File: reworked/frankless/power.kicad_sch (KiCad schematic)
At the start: 34 parts, among them J4 SS-52100-004, J5 USB4215-03-A, U1 TS3USB221RSER, U11 CH334R, U2 USBLC6-2SC6, U3 AMS1117-3.3, Y2 12Mhz, Y3 ASE-12MHz

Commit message: Patch a few minor issues.
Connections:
- net +3V3: no longer C39.2, C40.2, U11.13 (VDD33_{LDO})
- new net: C39.2, C40.2, U11.13 (VDD33_{LDO})
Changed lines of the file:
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@@
 	)
 	(junction
-		(at 130.81 110.49)
-		(diameter 0)
-		(color 0 0 0 0)
-	)
-	(junction
 		(at 27.94 123.19)
 		(diameter 0)
@@
 	(wire
 		(pts
-			(xy 129.54 110.49) (xy 130.81 110.49)
-		)
-		(stroke
-			(width 0)
-			(type default)
-		)
-	)
-	(wire
-		(pts
 			(xy 125.73 143.51) (xy 127 143.51)
 		)
@@
 					(unit 1)
 				)
-			)
-		)
-	)
-	(symbol
-		(lib_id "MicroFRANK:+3V3")
-		(at 129.54 110.49 0)
-		(unit 1)
-		(body_style 1)
-		(exclude_from_sim no)
-		(in_bom yes)
-		(on_board yes)
-		(in_pos_files yes)
-		(dnp no)
-		(fields_autoplaced yes)
-		(property "Reference" "#PWR011"
-			(at 129.54 114.3 0)
-			(hide yes)
-			(show_name no)
-			(do_not_autoplace no)
-			(effects
-				(font
-					(size 1.27 1.27)
-				)
-			)
-		)
-		(property "Value" "+3V3"
-			(at 129.54 105.41 0)
-			(show_name no)
-			(do_not_autoplace no)
-			(effects
-				(font
-					(size 1.27 1.27)
-				)
-			)
-		)
-		(property "Footprint" ""
-			(at 129.54 110.49 0)
-			(hide yes)
-			(show_name no)
-			(do_not_autoplace no)
-			(effects
-				(font
-					(size 1.27 1.27)
-				)
-			)
-		)
-		(property "Datasheet" ""
-			(at 129.54 110.49 0)
-			(hide yes)
-			(show_name no)
-			(do_not_autoplace no)
-			(effects
-				(font
-					(size 1.27 1.27)
-				)
-			)
-		)
-		(property "Description" "Power symbol creates a global label with name \"+3V3\""
-			(at 129.54 110.49 0)
-			(hide yes)
-			(show_name no)
-			(do_not_autoplace no)
-			(effects
-				(font
-					(size 1.27 1.27)
-				)
-			)
-		)
-		(pin "1"
-		)
-		(instances
-			(project "frankless"
-				(path "/8c0b3d8b-46d3-4173-ab1e-a61765f77d61/84d5e8f7-bda8-4f18-8ff8-1a8273c38b01"
-					(reference "#PWR011")
-					(unit 1)
-				)

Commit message: Patch a few minor issues.
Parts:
- L1: AliExpress https://jlcpcb.com/partdetail/Sunlord-GZ1005D331TF/C74324 -> https://jlcpcb.com/partdetail/MurataElectronics-BLM18PG121S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; LCSC Part # C74324 -> C14709
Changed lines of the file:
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@@
 			)
 		)
-		(property "AliExpress" "https://jlcpcb.com/partdetail/Sunlord-GZ1005D331TF/C74324"
+		(property "AliExpress" "https://jlcpcb.com/partdetail/MurataElectronics-BLM18PG121SN1D/C14709"
 			(at 261.62 71.12 0)
 			(hide yes)
@@
 			)
 		)
-		(property "LCSC Part #" "C74324"
+		(property "LCSC Part #" "C14709"
 			(at 261.62 71.12 90)
 			(hide yes)

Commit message: Fix a few parts.
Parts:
- R9: LCSC Part # C25905 -> C11702
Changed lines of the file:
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@@
 			)
 		)
-		(property "LCSC Part #" "C25905"
+		(property "LCSC Part #" "C11702"
 			(at 148.59 36.83 90)
 			(hide yes)

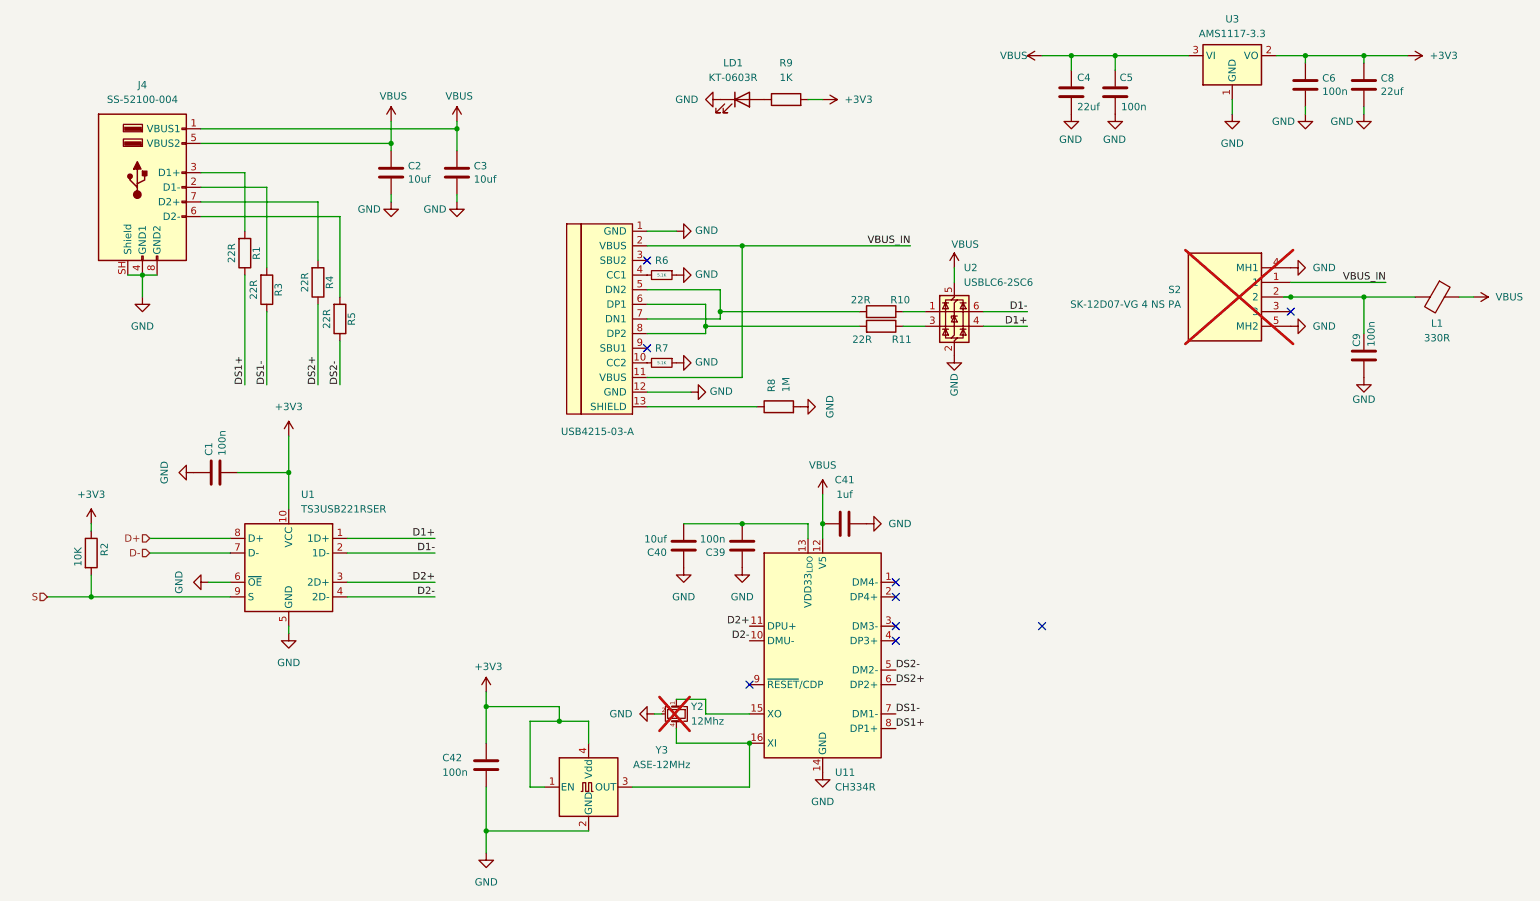
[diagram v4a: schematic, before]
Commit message: Fixing bad footprint matches.
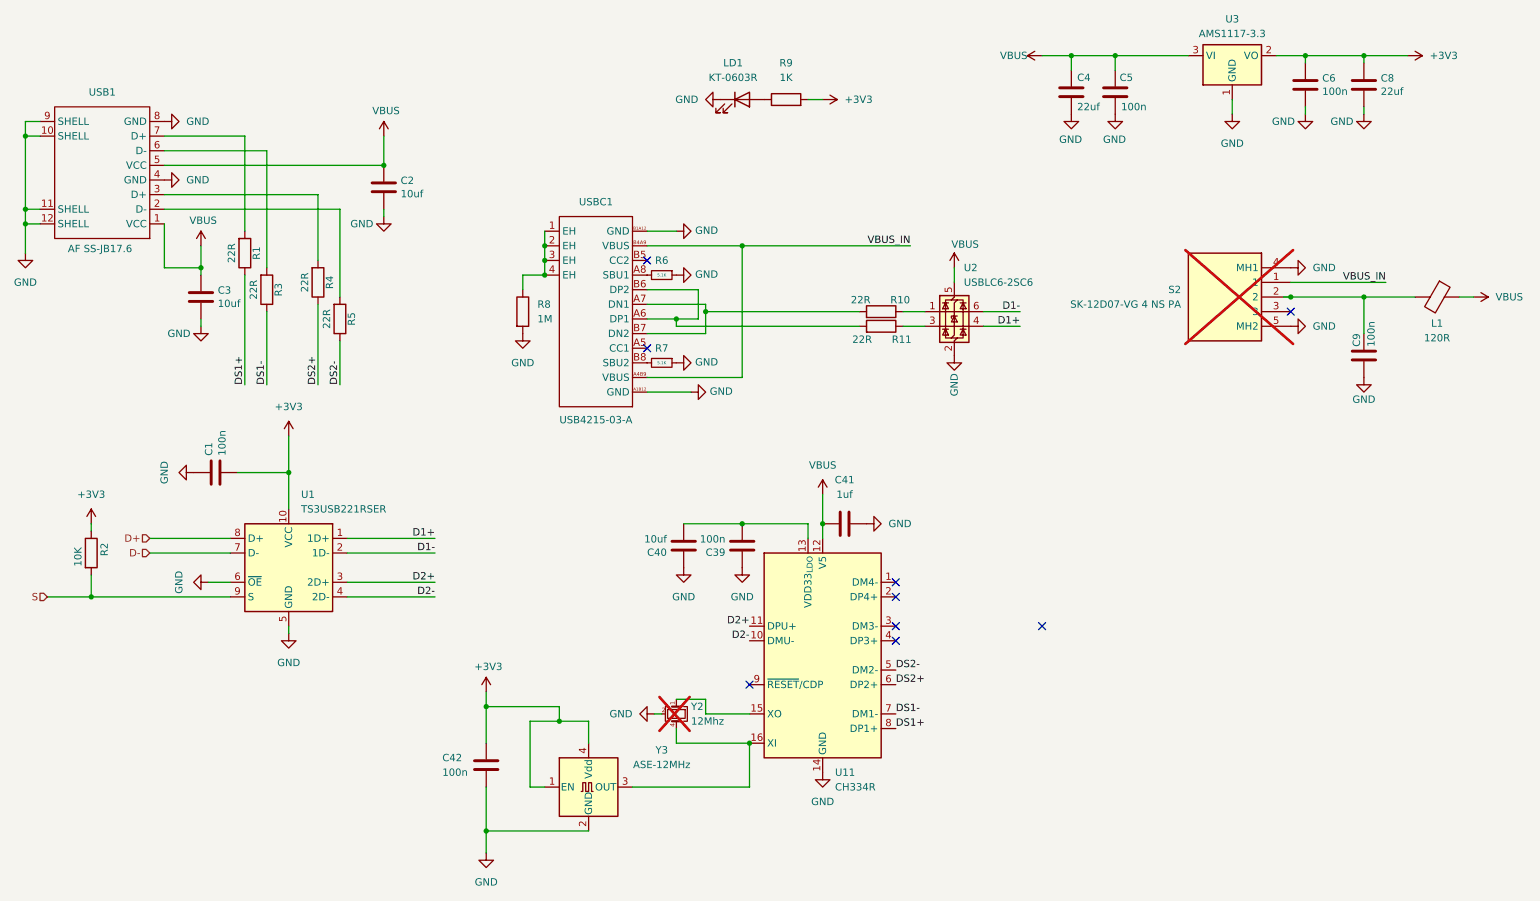
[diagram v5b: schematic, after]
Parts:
- removed J4: SS-52100-004, MicroFRANK:USB_A_Stacked, symbol MicroFRANK:USB_A_Stacked
- removed J5: USB4215-03-A, MicroFRANK:USB_C_Receptacle, symbol MicroFRANK:USB-C
- added USB1: AF SS-JB17.6, EasyEDA_Lib:USB-A-TH_AF-SS-JB17.6, symbol EasyEDA_Lib:AF SS-JB17.6
- added USBC1: USB4215-03-A, EasyEDA_Lib:USB-C_SMD-TYPE-C-31-M-12_1, symbol EasyEDA_Lib:TYPE-C-31-M-12
- L1: value 330R -> 120R
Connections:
- net GND: now also USB1.10 (SHELL), USB1.11 (SHELL), USB1.12 (SHELL), USB1.4 (GND), USB1.8 (GND), USB1.9 (SHELL), USBC1.A1B12 (GND), USBC1.B1A12 (GND)
- net VBUS: now also USB1.1 (VCC), USB1.5 (VCC)
- net VBUS_IN: now also USBC1.A4B9 (VBUS), USBC1.B4A9 (VBUS)
- net at R8.1: now also USBC1.1 (EH), USBC1.2 (EH), USBC1.3 (EH), USBC1.4 (EH)
- net at R3.2: now also USB1.6 (D-)
- net at R1.2: now also USB1.7 (D+)
- net at R5.2: now also USB1.2 (D-)
- net at R4.2: now also USB1.3 (D+)
- net at R7.2: now also USBC1.B8 (SBU2)
- net at R6.2: now also USBC1.A8 (SBU1)
- net at R10.2: now also USBC1.A7 (DN1), USBC1.B7 (DN2)
- net at R11.2: now also USBC1.A6 (DP1), USBC1.B6 (DP2)
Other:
- moved on the sheet: C2, C3, R8

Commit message: Fixing bad footprint matches.
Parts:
- removed USBC1: USB4215-03-A, EasyEDA_Lib:USB-C_SMD-TYPE-C-31-M-12_1, symbol EasyEDA_Lib:TYPE-C-31-M-12
- added USB2: USB4215-03-A, EasyEDA_Lib:USB-C-SMD_GT-USB-7010B, symbol EasyEDA_Lib:USB4215-03-A
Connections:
- net GND: now also USB2.A1B12 (GND), USB2.B1A12 (GND)
- net VBUS_IN: now also USB2.A4B9 (VBUS), USB2.B4A9 (VBUS)
- net at R8.1: now also USB2.13 (EH), USB2.14 (EH), USB2.15 (EH), USB2.16 (EH)
- net at R11.2: now also USB2.A6 (Dp1), USB2.B6 (Dp2)
- net at R10.2: now also USB2.A7 (Dn1), USB2.B7 (Dn2)
- net at R6.2: now also USB2.B5 (CC2)
- net at R7.2: now also USB2.A5 (CC1)
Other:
- moved on the sheet: R6, R7, R8

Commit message: More PCB layout clean ups.
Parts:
- added C7: 10uf, Capacitor_SMD:C_0603_1608Metric, symbol MicroFRANK:C
- C4: value 22uf -> 10uf; AliExpress https://jlcpcb.com/partdetail/60514-CL10A226MQ8NRNC/C59461 -> https://jlcpcb.com/partdetail/97651-CL10A106MA8NRNC/C96446; LCSC Part # C59461 -> C96446
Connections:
- net GND: now also C7.1
- net VBUS: now also C7.2
